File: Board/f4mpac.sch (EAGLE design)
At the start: 53 parts, among them CN1 DIP40 MB CONN, IC1 YM2413, IC10 27C512AL, IC2 74LS30D, IC3 74LS04D, IC4 LM4558N, IC5 Z80, IC6 74LS30D, IC7 74LS02D, IC8 74LS74D, IC9 74LS125D

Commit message: Release 23.01.2019
Improved board, redrawn schematics
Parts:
- removed C15: 100nF, rcl:C-EUC0805
- removed R16: 68, rcl:R-EU_R0805
- removed VREG2: 7805L, linear:7805L
- added R18: 1k, rcl:R-EU_R0805
- added SJ3: (no value), jumper:SJ
- C10, C13: value 1uF 25v -> 100nF; device rcl:CPOL-EUSMCB -> rcl:C-EUC0805
- R4: value 2.2k -> 4.7k
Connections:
- net N$2 renamed AMP
- net N$5 renamed +12VAMP
- net N$8 renamed -12VAMP
- removed net N$22 (its old number): C13.+, R16.1, VREG2.VI
- removed net N$23: C12.+, C15.2, IC1.16, VREG1.VO
- removed net VCC: CN1.11, IC5.VCC
- new net +5V: C10.1, C11.1, C13.1, CN1.11, D1.C, IC10.VCC, IC2P.VCC, IC3P.VCC, IC5.VCC, IC6P.VCC, IC7P.VCC, IC8A.CLR, IC8P.VCC, IC9B.I, IC9P.VCC, R15.1, R17.1, SJ2.1
- new net SLT: JP3.1, R18.2
- net +12V: no longer R16.2
- net +5VREG: now also C12.+, IC1.16, VREG1.VO; no longer C10.+, C11.1, D1.C, IC10.VCC, IC2P.VCC, IC3P.VCC, IC6P.VCC, IC7P.VCC, IC8A.CLR, IC8P.VCC, IC9B.I, IC9P.VCC, R15.1, R17.1, SJ2.1, VREG2.VO
- net GND: now also C10.2, C13.2, IC3A.I, IC3E.I, IC3F.I, IC9C.I, IC9C.OE, IC9D.I, IC9D.OE, SJ3.1, SJ3.2; no longer C10.-, C13.-, C15.1, VREG2.GND
- net N$40: now also R18.1; no longer JP3.1
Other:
- note added: "Board and optimizations by RBSC (2016-2018)"
- note added: "Digital and analogue GND separation"
- note added: "F4 Port + FMPAC Light (Mono)"
- note added: "F4 Port Register"
- note added: "Motherboard Z80 Socket"
- note added: "Z80 CPU"
- note removed: "/IORQ"
- note removed: "/M1"
- note removed: "/RD"
- note removed: "/WR"
- note removed: "A0"
- note removed: "A1"
- note removed: "A2"
- note removed: "A3"
- note removed: "A4"
- note removed: "A5"
- note removed: "A6"
- note removed: "A7"
- note removed: "Board and optimizations by RBSC (2016)"
- note removed: "D7"
- note removed: "F4 Port + FMPAC"
- note removed: "F4 Register"
- note removed: "Motherboard Connector"
- note removed: "Z80"
- moved on the sheet: C1, C11, C12, C14, C16, C2, C3, C4, C5, C6, C7, C8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

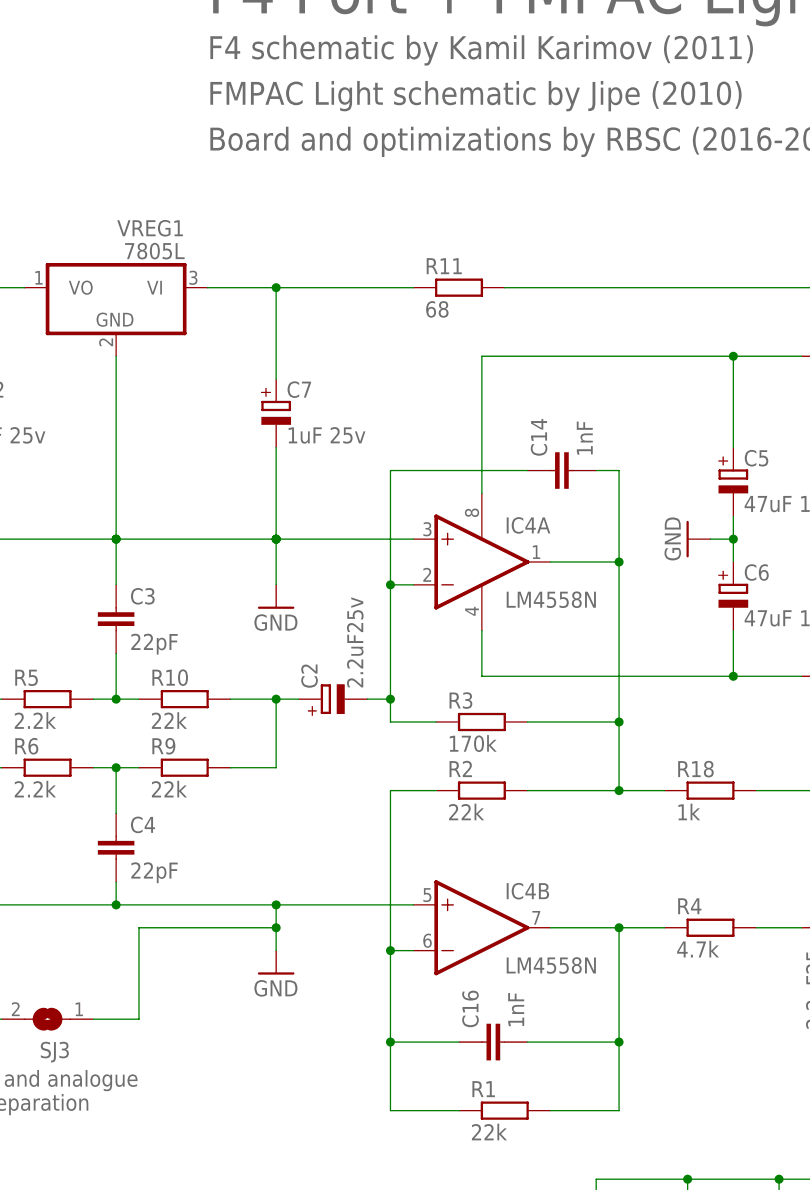
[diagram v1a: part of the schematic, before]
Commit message: Updated 14.05.2025
Updated the board to version 1.5. Corrected R4, C14 and C16 values. Updated readme file.
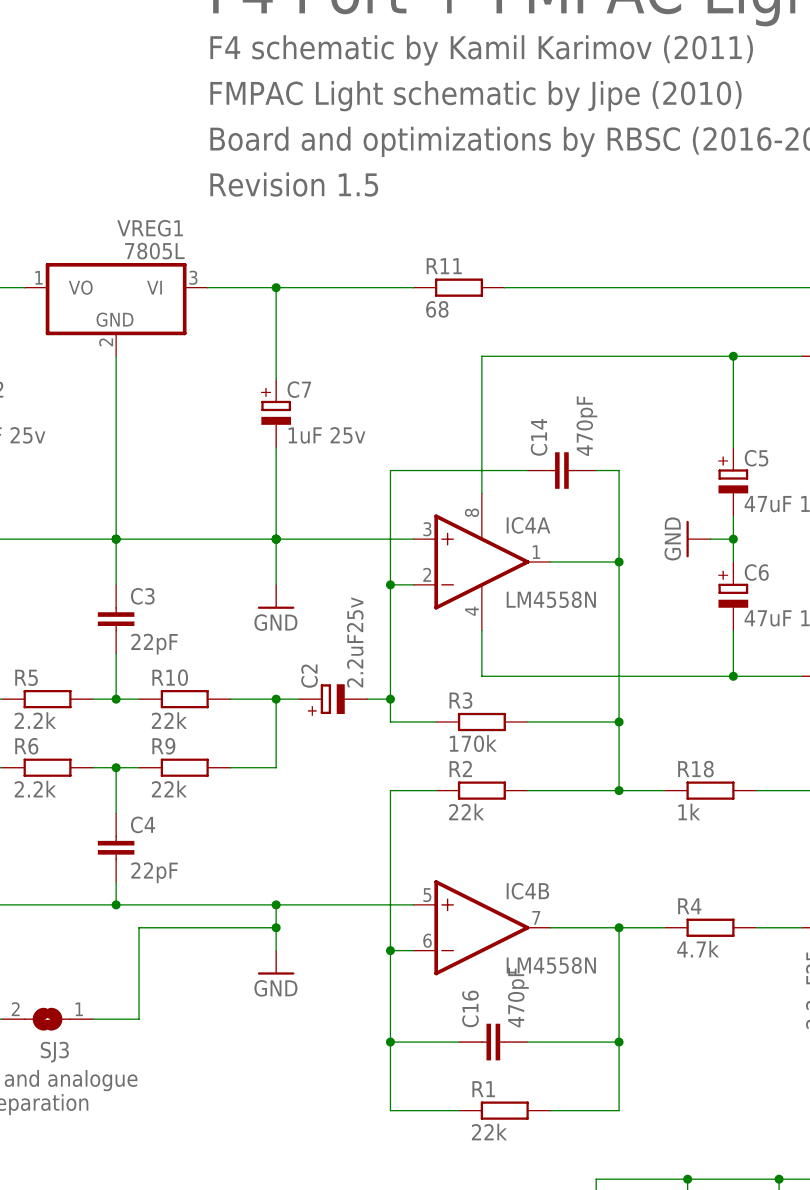
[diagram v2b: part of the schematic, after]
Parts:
- C14, C16: value 1nF -> 470pF
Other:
- note added: "Revision 1.5"
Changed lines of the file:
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@@
 <part name="GND10" library="supply1" deviceset="GND" device=""/>
 <part name="JP2" library="pinhead" deviceset="PINHD-1X2" device="/90" value="OE/CE"/>
-<part name="C14" library="rcl" deviceset="C-EU" device="C0805" value="1nF"/>
+<part name="C14" library="rcl" deviceset="C-EU" device="C0805" value="470pF"/>
 <part name="C8" library="rcl" deviceset="C-EU" device="C0805" value="100nF"/>
 <part name="GND14" library="supply1" deviceset="GND" device=""/>
-<part name="C16" library="rcl" deviceset="C-EU" device="C0805" value="1nF"/>
+<part name="C16" library="rcl" deviceset="C-EU" device="C0805" value="470pF"/>
 <part name="IC10" library="microchip" deviceset="27*512A" device="L" technology="C"/>
 <part name="SJ2" library="jumper" deviceset="SJ2W" device=""/>
@@
 <text x="88.9" y="5.08" size="1.778" layer="95">Digital and analogue
 GND separation</text>
+<text x="119.38" y="106.68" size="2.54" layer="95">Revision 1.5</text>
 </plain>
 <instances>
